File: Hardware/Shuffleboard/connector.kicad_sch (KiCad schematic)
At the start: 2 parts, among them J1 1751138, J2 1751138

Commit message: led's, mux
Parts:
- removed J1, J2: 1751138, 1751138, symbol ShuffCon:1751138
- added J1, J2: 1869279, 1869279, symbol ShuffCon:1869279
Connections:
- net 3.3VIN: now also J1.1
- net GNDIN: now also J1.8
- net HOR_PB18_ADC1_5: now also J1.6
- net PA15_DAC_OUT: now also J1.2
- net PB1_RST: now also J1.4
- net PB4_SHOOT: now also J1.3
- net POS_PB17_ADC1_4: now also J1.5
- net VER_PB19_ADC1_6: now also J1.7
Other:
- note added: "Inputs/Speaker/Power"
- note added: "Screen/8Segment"

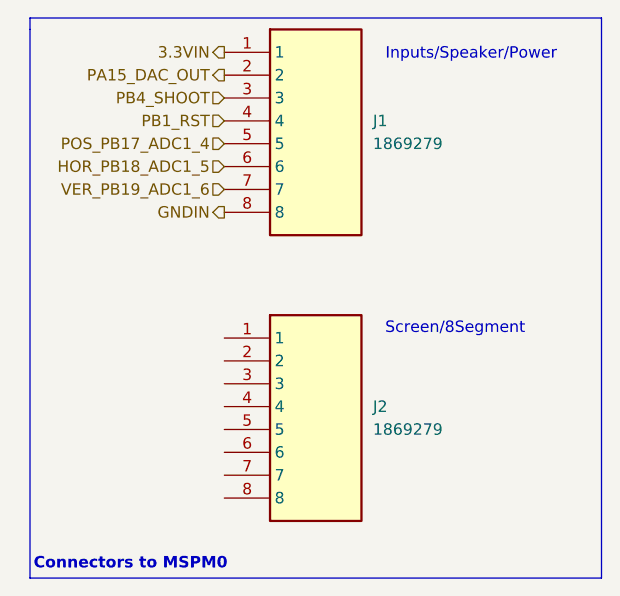
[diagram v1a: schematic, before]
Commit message: implemented 7-seg
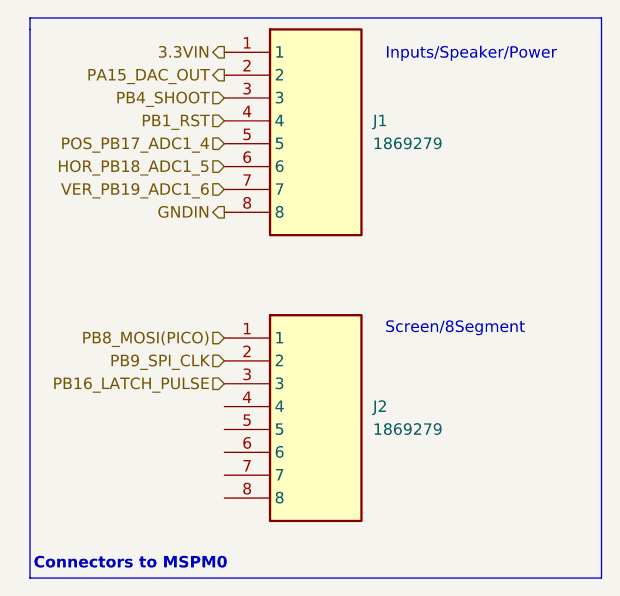
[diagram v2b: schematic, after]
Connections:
- net PB8_MOSI(PICO): now reaches J2.1
- net PB9_SPI_CLK: now reaches J2.2
- net PB16_LATCH_PULSE: now reaches J2.3
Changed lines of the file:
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@@
+		)
+	)
+	(hierarchical_label "PB8_MOSI(PICO)"
+		(shape input)
+		(at 39.37 50.8 180)
+		(effects
+			(font
+				(size 1.27 1.27)
+			)
+			(justify right)
 		)
 	)
@@
 				(size 1.27 1.27)
 				(thickness 0.1588)
+			)
+			(justify right)
+		)
+	)
+	(hierarchical_label "PB9_SPI_CLK"
+		(shape input)
+		(at 39.37 53.34 180)
+		(effects
+			(font
+				(size 1.27 1.27)
 			)
 			(justify right)
@@
 		(effects
 			(font
+				(size 1.27 1.27)
+			)
+			(justify right)
+		)
+	)
+	(hierarchical_label "PB16_LATCH_PULSE"
+		(shape input)
+		(at 39.37 55.88 180)
+		(effects
+			(font

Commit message: layout
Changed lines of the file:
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@@
 	)
 	(hierarchical_label "PB8_MOSI(PICO)"
-		(shape input)
+		(shape output)
 		(at 39.37 50.8 180)
 		(effects
@@
 	)
 	(hierarchical_label "PB9_SPI_CLK"
-		(shape input)
+		(shape output)
 		(at 39.37 53.34 180)
 		(effects
@@
 	)
 	(hierarchical_label "PB16_LATCH_PULSE"
-		(shape input)
+		(shape output)
 		(at 39.37 55.88 180)
 		(effects

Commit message: Finished Screen
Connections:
- net GNDIN: now also J2.8
- net PB7_MISO(POCI): now reaches J2.4
- net PB6_TFT_CS: now reaches J2.5
- net PA13_DC: now reaches J2.6
- net PB15_RESET: now reaches J2.7
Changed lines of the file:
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@@
+		)
+	)
+	(hierarchical_label "PB7_MISO(POCI)"
+		(shape output)
+		(at 39.37 58.42 180)
+		(effects
+			(font
+				(size 1.27 1.27)
+			)
+			(justify right)
 		)
 	)
@@
 		(shape output)
 		(at 39.37 19.05 180)
+		(effects
+			(font
+				(size 1.27 1.27)
+			)
+			(justify right)
+		)
+	)
+	(hierarchical_label "PB15_RESET"
+		(shape output)
+		(at 39.37 66.04 180)
 		(effects
 			(font
@@
 		)
 	)
+	(hierarchical_label "PB6_TFT_CS"
+		(shape output)
+		(at 39.37 60.96 180)
+		(effects
+			(font
+				(size 1.27 1.27)
+			)
+			(justify right)
+		)
+	)
+	(hierarchical_label "PA13_DC"
+		(shape output)
+		(at 39.37 63.5 180)
+		(effects
+			(font
+				(size 1.27 1.27)
+			)
+			(justify right)
+		)
+	)
 	(hierarchical_label "PB16_LATCH_PULSE"
 		(shape output)
@@
 			)
 			(justify right)
+		)
+	)
+	(hierarchical_label "GNDIN"
+		(shape output)
+		(at 39.37 68.58 180)
+		(effects
+			(font
+				(size 1.27 1.27)
+			)
+			(justify right)

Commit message: finished layout
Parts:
- removed J1, J2: 1869279, 1869279, symbol ShuffCon:1869279
- added J1, J2: TBJ05-08-1-G-G, ShuffleboardFootprints:TBJ05081GG, symbol Shuffle:TBJ05-08-1-G-G
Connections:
- net 3.3VIN: now also J1.1
- net GNDIN: now also J1.8, J2.8
- net HOR_PB18_ADC1_5: now also J1.6
- net PA13_DC: now also J2.6
- net PA15_DAC_OUT: now also J1.2
- net PB15_RESET: now also J2.7
- net PB16_LATCH_PULSE: now also J2.3
- net PB1_RST: now also J1.4
- net PB4_SHOOT: now also J1.3
- net PB6_TFT_CS: now also J2.5
- net PB7_MISO(POCI): now also J2.4
- net PB8_MOSI(PICO): now also J2.1
- net PB9_SPI_CLK: now also J2.2
- net POS_PB17_ADC1_4: now also J1.5
- net VER_PB19_ADC1_6: now also J1.7

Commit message: tht resistors
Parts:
- J1, J2: Mouser Link (none) -> https://www.mouser.com/ProductDetail/GCT/TBJ05-08-1-G-G?qs=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; Mouser Part Number (none) -> 640-TBJ05-08-1-G-G
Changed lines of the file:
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@@
 			)
 		)
-		(property "Mouser Part Number" ""
+		(property "Mouser Part Number" "640-TBJ05-08-1-G-G"
 			(at 55.88 513.97 0)
 			(hide yes)
@@
 				)
 				(justify left top)
+			)
+		)
+		(property "Mouser Link" "https://www.mouser.com/ProductDetail/GCT/TBJ05-08-1-G-G?qs=bN4HulGPsrEv0OFHcnyVFQ%3D%3D"
+			(at 39.37 19.05 0)
+			(hide yes)
+			(show_name no)
+			(do_not_autoplace no)
+			(effects
+				(font
+					(size 1.27 1.27)
+				)
+			)
+		)
+		(property "VALUE" ""
+			(at 39.37 19.05 0)
+			(hide yes)
+			(show_name no)
+			(do_not_autoplace no)
+			(effects
+				(font
+					(size 1.27 1.27)
+				)
 			)
 		)
@@
 			)
 		)
-		(property "Mouser Part Number" ""
+		(property "Mouser Part Number" "640-TBJ05-08-1-G-G"
 			(at 55.88 545.72 0)
 			(hide yes)
@@
 			)
 		)
+		(property "Mouser Link" "https://www.mouser.com/ProductDetail/GCT/TBJ05-08-1-G-G?qs=bN4HulGPsrEv0OFHcnyVFQ%3D%3D"
+			(at 39.37 50.8 0)
+			(hide yes)
+			(show_name no)
+			(do_not_autoplace no)
+			(effects
+				(font
+					(size 1.27 1.27)
+				)
+			)
+		)
+		(property "VALUE" ""
+			(at 39.37 50.8 0)
+			(hide yes)
+			(show_name no)
+			(do_not_autoplace no)
+			(effects
+				(font
+					(size 1.27 1.27)
+				)
+			)
+		)

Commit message: updated to end
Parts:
- J1, J2: value TBJ05-08-1-G-G -> (none)
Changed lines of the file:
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@@
 			)
 		)
-		(property "Value" "TBJ05-08-1-G-G"
-			(at 55.88 29.2099 0)
-			(show_name no)
-			(do_not_autoplace no)
-			(effects
-				(font
-					(size 1.27 1.27)
-				)
-				(justify left)
+		(property "Value" ""
+			(at 39.37 19.05 0)
+			(hide yes)
+			(show_name no)
+			(do_not_autoplace no)
+			(effects
+				(font
+					(size 1.27 1.27)
+				)
 			)
 		)
@@
 		)
 		(property "Mouser Link" "https://www.mouser.com/ProductDetail/GCT/TBJ05-08-1-G-G?qs=bN4HulGPsrEv0OFHcnyVFQ%3D%3D"
-			(at 39.37 19.05 0)
-			(hide yes)
-			(show_name no)
-			(do_not_autoplace no)
-			(effects
-				(font
-					(size 1.27 1.27)
-				)
-			)
-		)
-		(property "VALUE" ""
 			(at 39.37 19.05 0)
 			(hide yes)
@@
 			)
 		)
-		(property "Value" "TBJ05-08-1-G-G"
-			(at 55.88 60.9599 0)
-			(show_name no)
-			(do_not_autoplace no)
-			(effects
-				(font
-					(size 1.27 1.27)
-				)
-				(justify left)
+		(property "Value" ""
+			(at 39.37 50.8 0)
+			(hide yes)
+			(show_name no)
+			(do_not_autoplace no)
+			(effects
+				(font
+					(size 1.27 1.27)
+				)
 			)
 		)
@@
 			(at 39.37 50.8 0)
 			(hide yes)
-			(show_name no)
-			(do_not_autoplace no)
-			(effects
-				(font
-					(size 1.27 1.27)
-				)
-			)
-		)
-		(property "VALUE" ""
-			(at 39.37 50.8 0)
-			(hide yes)
